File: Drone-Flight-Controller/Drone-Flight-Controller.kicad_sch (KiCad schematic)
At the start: 62 parts, among them J10 TestPoint, J11 TestPoint, J12 TestPoint, J13 TestPoint, J14 TestPoint, J2 Raspberry_Pi_4, J3 TestPoint, J4 TestPoint, J5 TestPoint, J6 TestPoint, J7 TestPoint, J8 TestPoint, J9 TestPoint, Q1 BSS138, Q2 BSS138, Q3 BSS138, Q4 BSS138, SW1 SW_Omron_B3FS, U1 MCP1700x-180xxMB, U2 LMR51430, U3 ADC101C021CIMK, U4 ICM-20948, U5 BMP280, U6 PCA9531PW

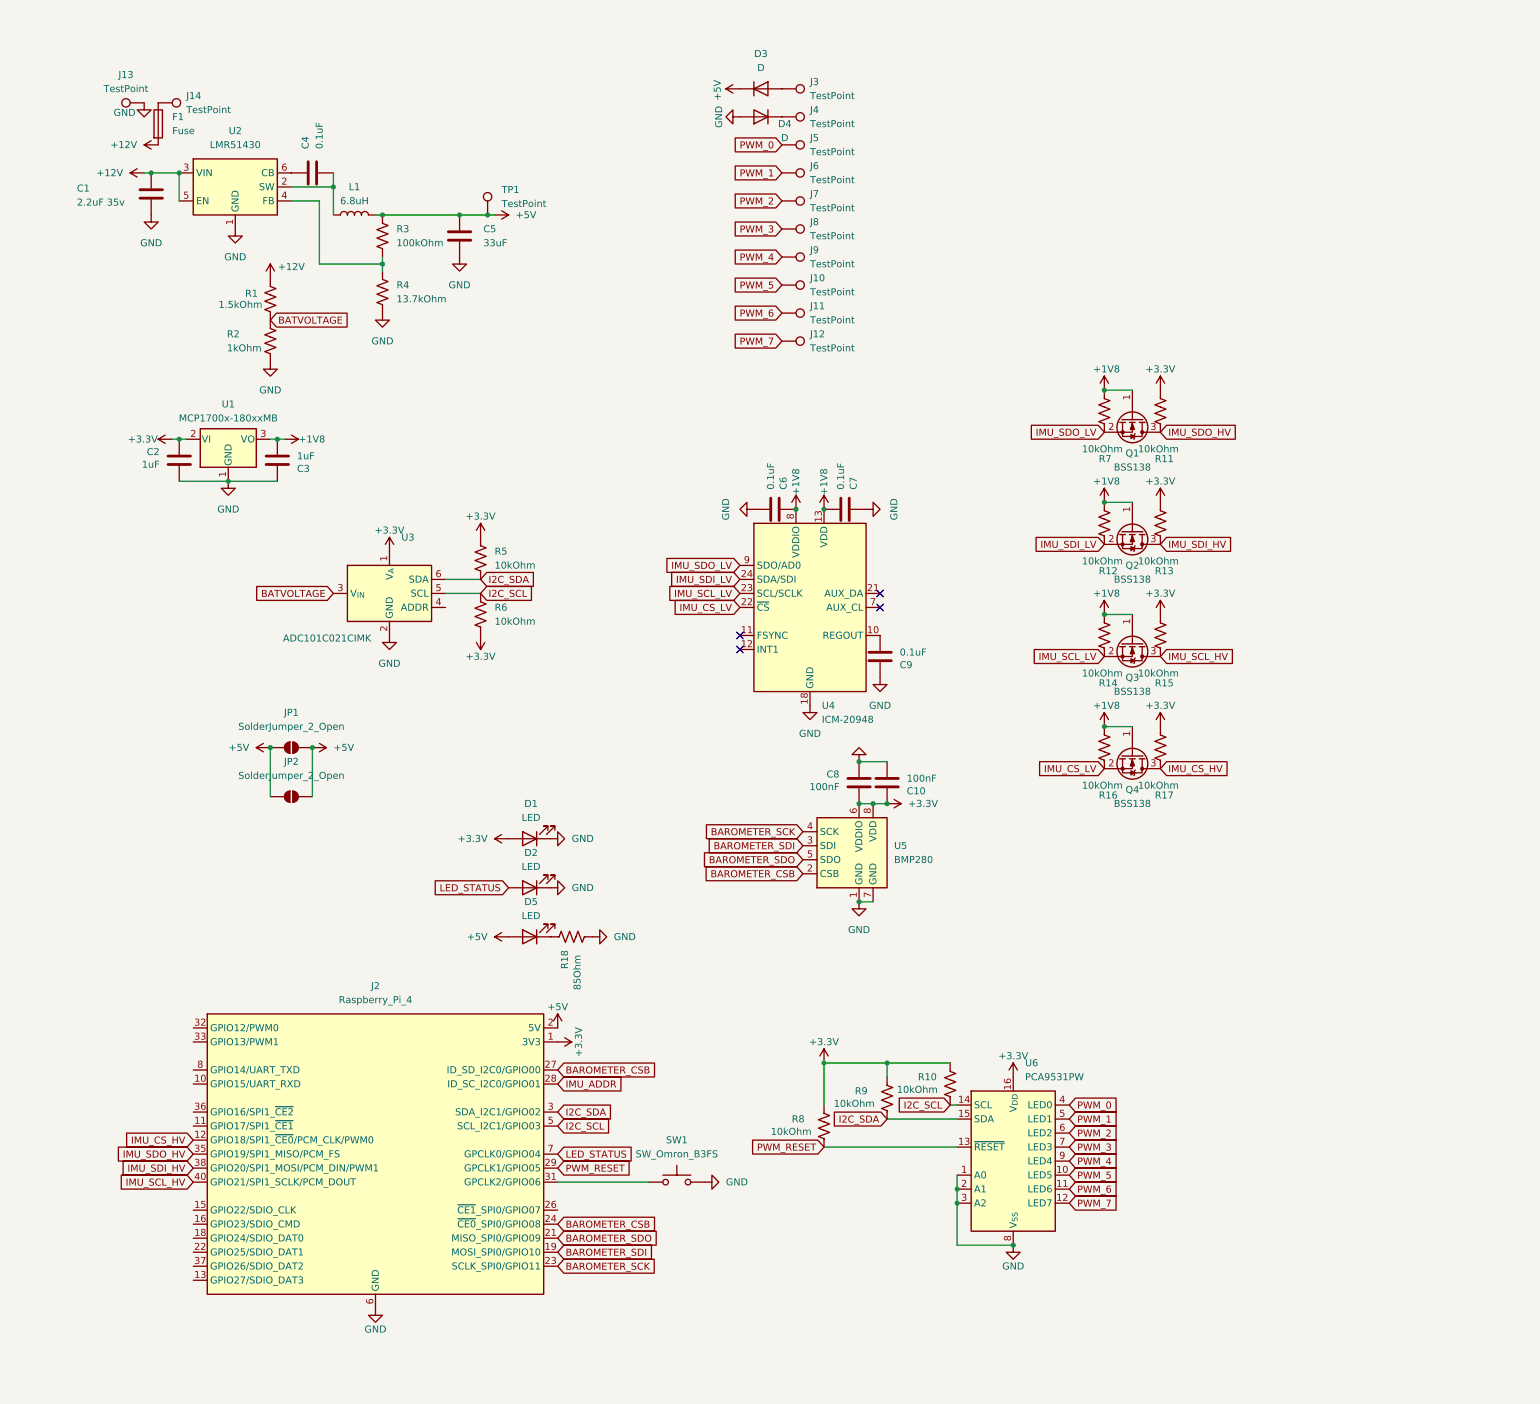
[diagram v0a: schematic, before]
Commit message: connect imu and barometer to spi0
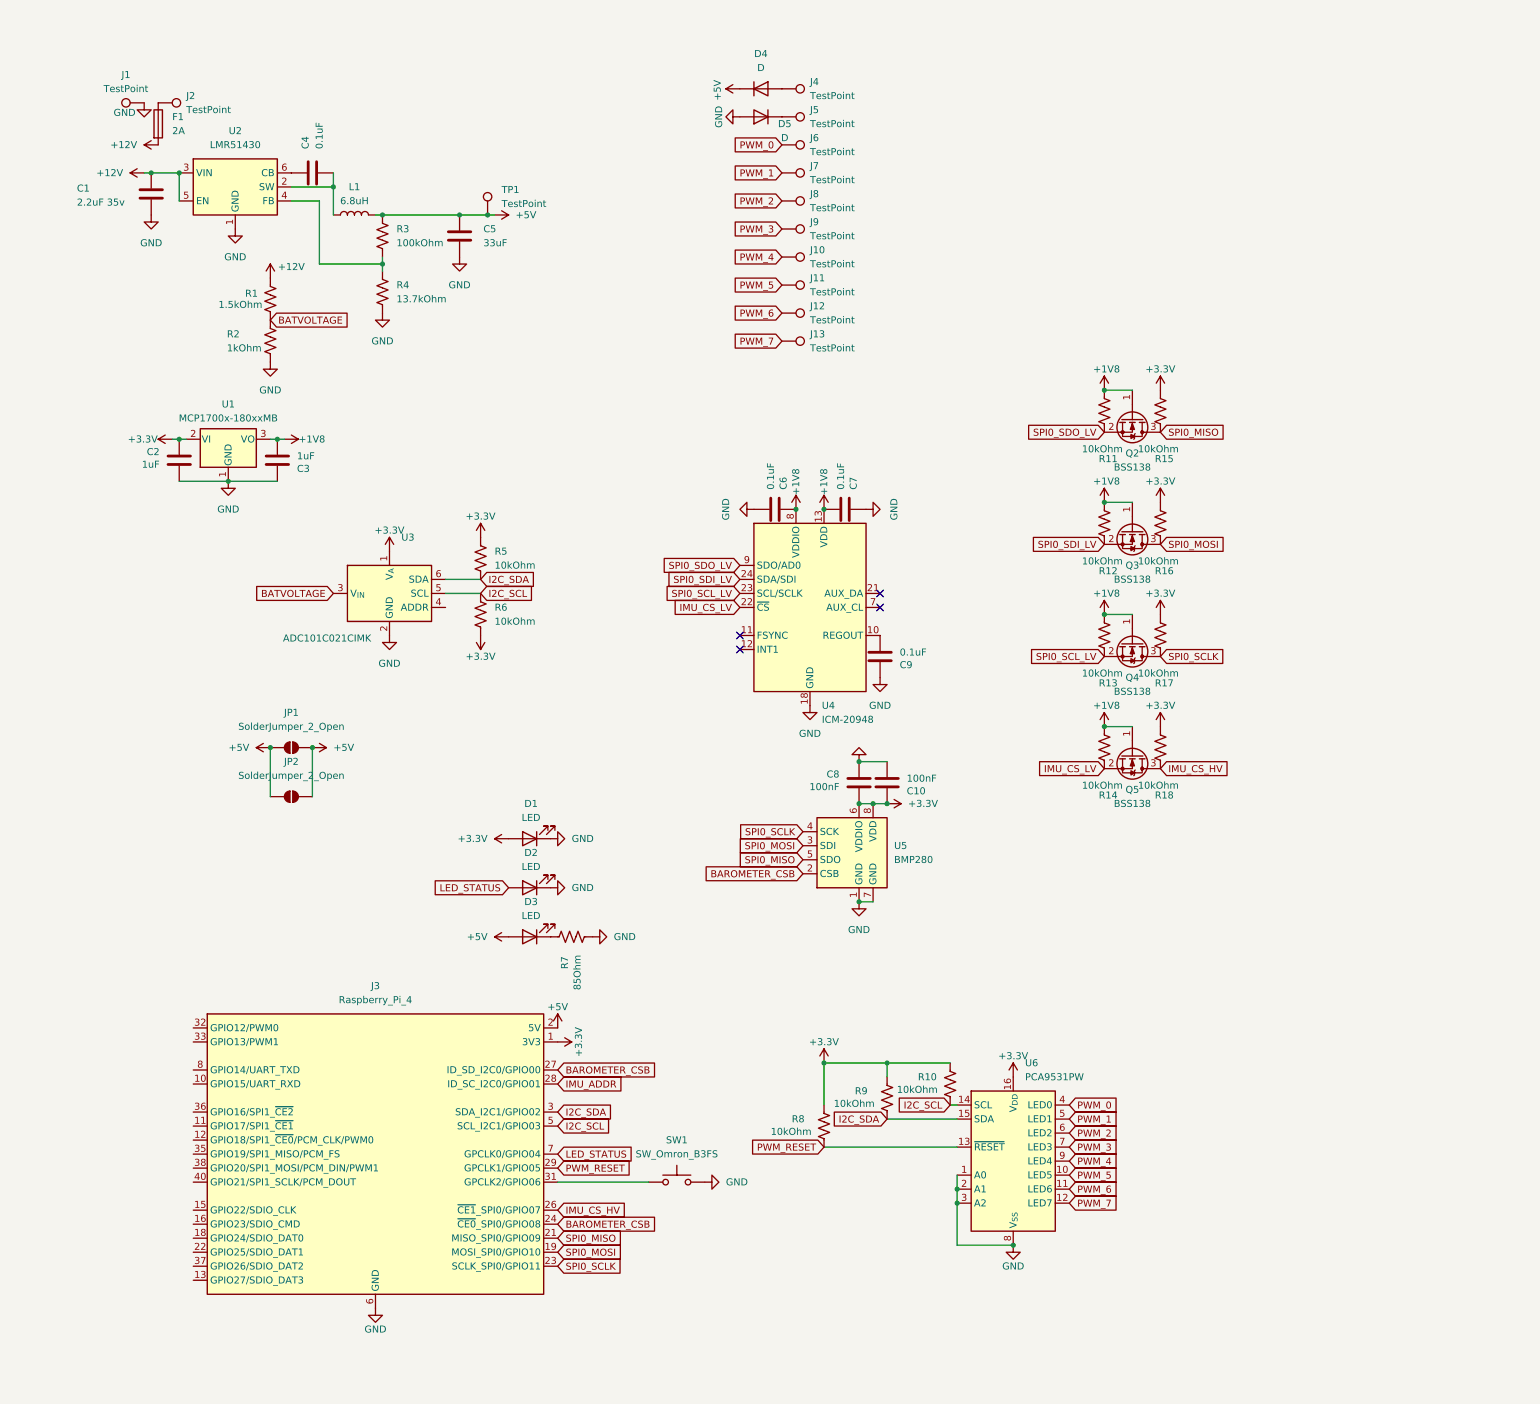
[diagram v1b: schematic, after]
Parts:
- F1: value Fuse -> 2A
- renumbered D5 to D3, D3 to D4, D4 to D5, J13 to J1, J9 to J10, J10 to J11, J11 to J12, J12 to J13, J14 to J2, J2 to J3, J3 to J4, J4 to J5, J5 to J6, J6 to J7, J7 to J8, J8 to J9, Q1 to Q2, Q2 to Q3, Q3 to Q4, Q4 to Q5, R7 to R11, R14 to R13, R16 to R14, R11 to R15, R13 to R16, R15 to R17, R17 to R18, R18 to R7
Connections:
- net IMU_CS_HV: now also J3.26 (~{CE1}_SPI0/GPIO07); no longer J3.12 (GPIO18/SPI1_~{CE0}/PCM_CLK/PWM0)
- net BAROMETER_SCK renamed SPI0_SCLK
- net SPI0_SCLK: now also Q4.3 (D), R17.1
- net BAROMETER_SDI renamed SPI0_MOSI
- net SPI0_MOSI: now also Q3.3 (D), R16.1
- net BAROMETER_SDO renamed SPI0_MISO
- net SPI0_MISO: now also Q2.3 (D), R15.1
- removed net IMU_SCL_HV: J3.40 (GPIO21/SPI1_SCLK/PCM_DOUT), Q4.3 (D), R17.1
- net IMU_SCL_LV renamed SPI0_SCL_LV
- removed net IMU_SDI_HV: J3.38 (GPIO20/SPI1_MOSI/PCM_DIN/PWM1), Q3.3 (D), R16.1
- net IMU_SDI_LV renamed SPI0_SDI_LV
- removed net IMU_SDO_HV: J3.35 (GPIO19/SPI1_MISO/PCM_FS), Q2.3 (D), R15.1
- net IMU_SDO_LV renamed SPI0_SDO_LV

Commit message: switch to bmp390 for barometer
bmp280 isnt being stocked at digikey or mouser anymore
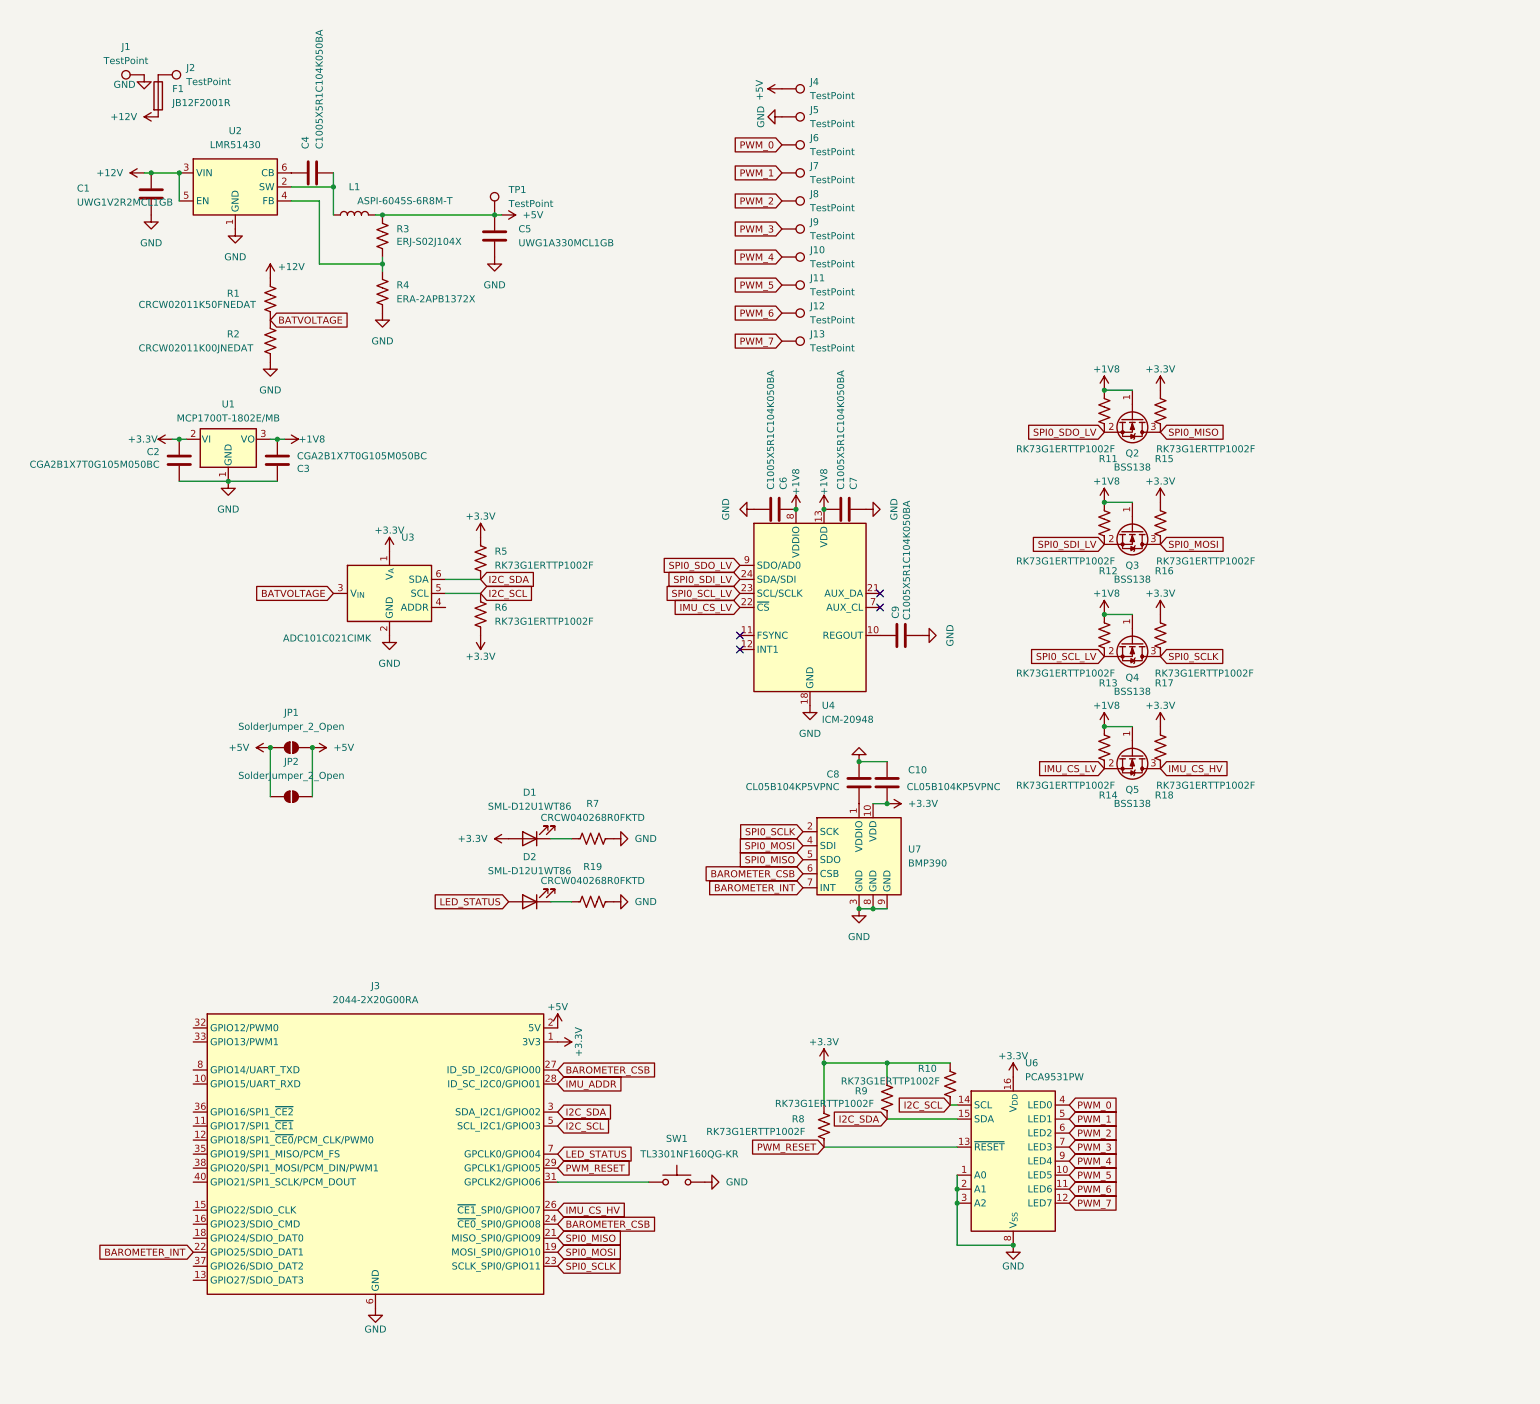
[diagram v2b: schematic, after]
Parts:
- removed D3: LED, LED_SMD:LED_0402_1005Metric, symbol Device:LED
- removed D4, D5: D, Diode_SMD:D_0805_2012Metric, symbol Device:D
- removed U5: BMP280, Package_LGA:Bosch_LGA-8_2x2.5mm_P0.65mm_ClockwisePinNumbering, symbol Sensor_Pressure:BMP280
- added R19: CRCW040268R0FKTD, Resistor_SMD:R_0402_1005Metric, symbol Device:R_US
- added U7: BMP390, Package_LGA:ST_HLGA-10_2x2mm_P0.5mm_LayoutBorder3x2y, symbol Sensor_Pressure:BMP390
- C1: value 2.2uF 35v -> UWG1V2R2MCL1GB; footprint Capacitor_SMD:C_0402_1005Metric -> Capacitor_SMD:C_Elec_4x5.4
- C10, C8: value 100nF -> CL05B104KP5VPNC
- C2, C3: value 1uF -> CGA2B1X7T0G105M050BC
- C4, C6, C7, C9: value 0.1uF -> C1005X5R1C104K050BA
- C5: value 33uF -> UWG1A330MCL1GB
- D1, D2: value LED -> SML-D12U1WT86; footprint LED_SMD:LED_0402_1005Metric -> LED_SMD:LED_0603_1608Metric
- F1: value 2A -> JB12F2001R
- J3: value Raspberry_Pi_4 -> 2044-2X20G00RA
- L1: value 6.8uH -> ASPI-6045S-6R8M-T
- R1: value 1.5kOhm -> CRCW02011K50FNEDAT
- R10, R11, R12, R13, R14, R15, R16, R17, R18, R5, R6, R8, R9: value 10kOhm -> RK73G1ERTTP1002F
- R2: value 1kOhm -> CRCW02011K00JNEDAT
- R3: value 100kOhm -> ERJ-S02J104X
- R4: value 13.7kOhm -> ERA-2APB1372X
- R7: value 85Ohm -> CRCW040268R0FKTD
- SW1: value SW_Omron_B3FS -> TL3301NF160QG-KR
- U1: value MCP1700x-180xxMB -> MCP1700T-1802E/MB
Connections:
- net +3.3V: now also U7.10 (VDD); no longer C8.1
- net +5V: now also J4.1
- net BAROMETER_CSB: now also U7.6 (CSB)
- net GND: now also J5.1, R19.2, U7.3 (GND), U7.8 (GND), U7.9 (GND); no longer D1.1 (K), D2.1 (K)
- net SPI0_MISO: now also U7.5 (SDO)
- net SPI0_MOSI: now also U7.4 (SDI)
- net SPI0_SCLK: now also U7.2 (SCK)
- net at R7.1: now also D1.1 (K)
- net BAROMETER_INT: now reaches J3.22 (GPIO25/SDIO_DAT1)
- net BAROMETER_INT: now also U7.7 (INT)
- new net: D2.1 (K), R19.1
- new net: C8.1, U7.1 (VDDIO)
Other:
- moved on the sheet: C5, C9, D2, F1, J1, J2, TP1

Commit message: i2c to pwm is now a pca9685
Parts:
- removed U6: PCA9531PW, Package_SO:TSSOP-16_4.4x5mm_P0.65mm, symbol Driver_LED:PCA9531PW
- added R10, R11, R13, R15, R16, R9: RK73G1ERTTP1002F, Resistor_SMD:R_0402_1005Metric, symbol Device:R_US
- added U6: PCA9685PW, Package_SO:TSSOP-28_4.4x9.7mm_P0.65mm, symbol Driver_LED:PCA9685PW
- renumbered C9 to C10, C10 to C9, Q2 to Q1, Q3 to Q2, Q4 to Q3, Q5 to Q4, R8 to R12, R9 to R14, R10 to R17, R11 to R18, R12 to R19, R13 to R20, R14 to R21, R15 to R22, R16 to R23, R17 to R24, R18 to R25, R19 to R8, U7 to U5
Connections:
- net +3.3V: now also U6.28 (VDD)
- net GND: now also R10.2, R11.2, R13.2, R15.2, R16.2, R9.2, U6.14 (VSS)
- net I2C_SCL: now also U6.26 (SCL)
- net I2C_SDA: now also U6.27 (SDA)
- net PWM_0: now also U6.6 (LED0)
- net PWM_1: now also U6.7 (LED1)
- net PWM_2: now also U6.8 (LED2)
- net PWM_3: now also U6.9 (LED3)
- net PWM_4: now also U6.10 (LED4)
- net PWM_5: now also U6.11 (LED5)
- net PWM_6: now also U6.12 (LED6)
- net PWM_7: now also U6.13 (LED7)
- net PWM_RESET: now also U6.23 (~{OE})
- new net: R11.1, U6.4 (A3)
- new net: R16.1, U6.1 (A0)
- new net: R15.1, U6.2 (A1)
- new net: R13.1, U6.3 (A2)
- new net: R9.1, U6.24 (A5)
- new net: R10.1, U6.5 (A4)
- no-connect marks 4 -> 5
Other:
- moved on the sheet: SW1

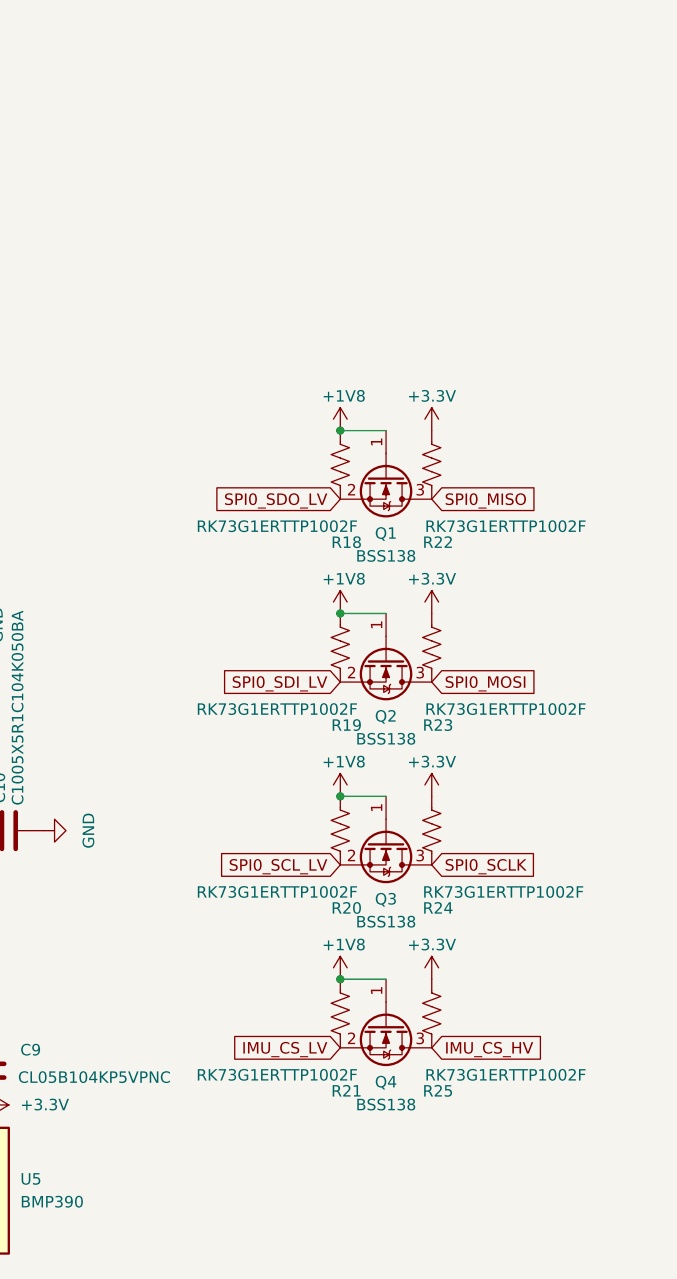
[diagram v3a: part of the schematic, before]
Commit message: level shifters are a single part now
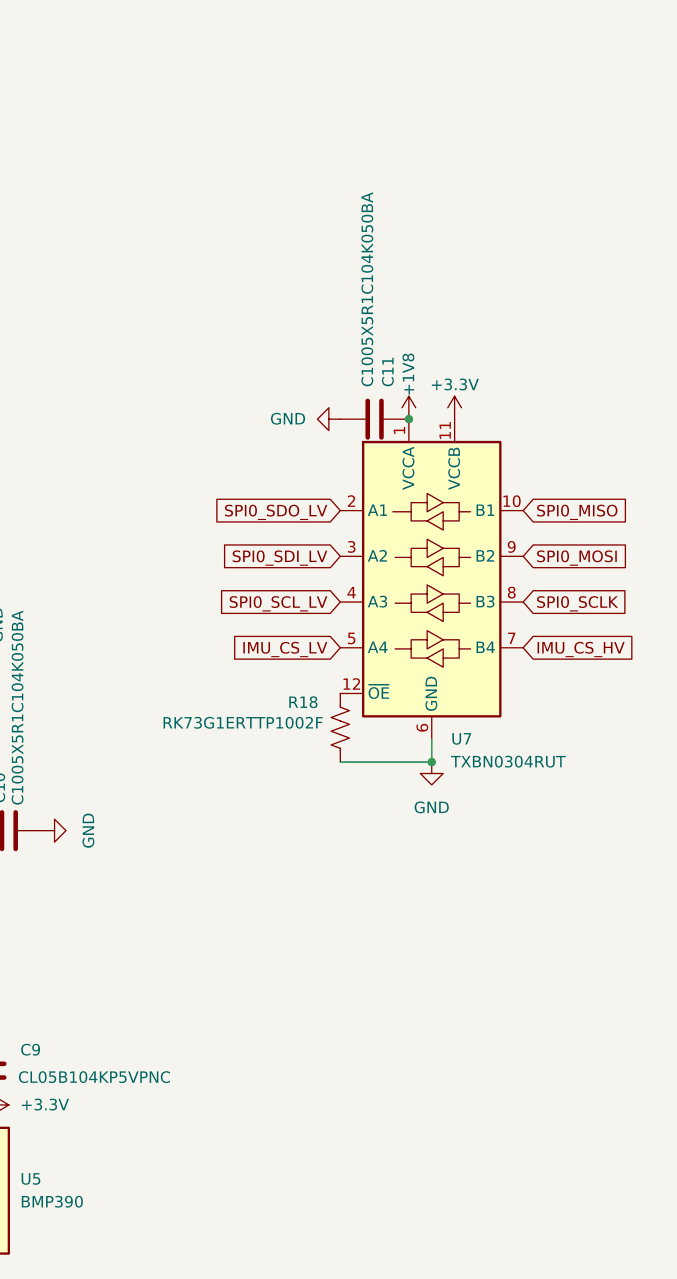
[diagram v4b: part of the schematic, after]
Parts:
- removed Q1, Q2, Q3, Q4: BSS138, Package_TO_SOT_SMD:SOT-23, symbol Transistor_FET:BSS138
- removed R19, R20, R21, R22, R23, R24, R25: RK73G1ERTTP1002F, Resistor_SMD:R_0402_1005Metric, symbol Device:R_US
- added C11: C1005X5R1C104K050BA, Capacitor_SMD:C_0402_1005Metric, symbol Device:C
- added U7: TXBN0304RUT, Package_DFN_QFN:Texas_R-PUQFN-N12, symbol Logic_LevelTranslator:TXBN0304RUT
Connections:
- net +1V8: now also C11.2, U7.1 (VCCA); no longer R18.2
- net +3.3V: now also U7.11 (VCCB)
- net GND: now also R18.2, C11.1, U7.6 (GND)
- net IMU_CS_HV: now also U7.7 (B4)
- net IMU_CS_LV: now also U7.5 (A4)
- net SPI0_MISO: now also U7.10 (B1)
- net SPI0_MOSI: now also U7.9 (B2)
- net SPI0_SCLK: now also U7.8 (B3)
- net SPI0_SCL_LV: now also U7.4 (A3)
- net SPI0_SDI_LV: now also U7.3 (A2)
- net SPI0_SDO_LV: now also U7.2 (A1); no longer R18.1
- new net: R18.1, U7.12 (~{OE})
